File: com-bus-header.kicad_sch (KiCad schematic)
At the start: 10 parts, among them IC6 SN75C3232EPWR, J2 67996-110HLF

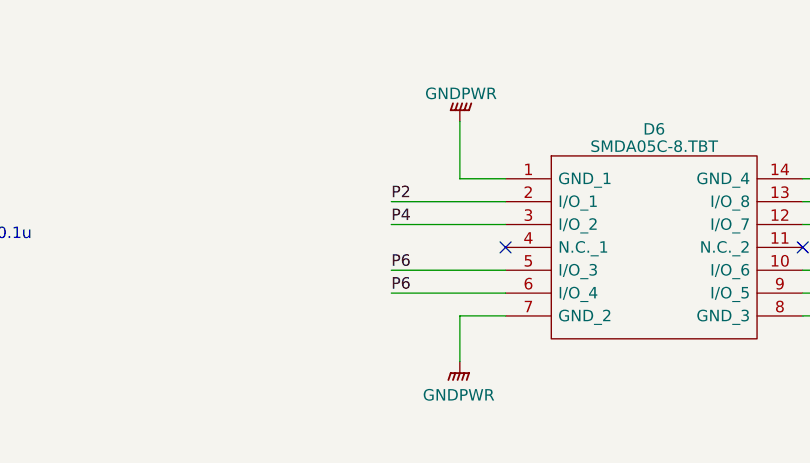
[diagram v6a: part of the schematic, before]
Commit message: initial component layout
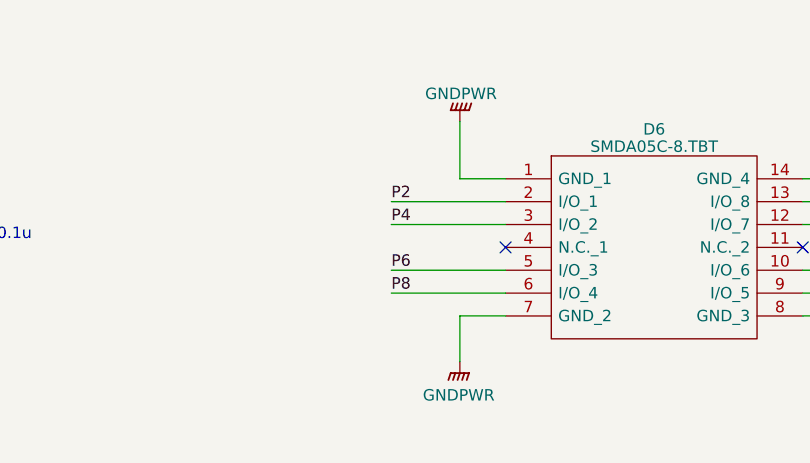
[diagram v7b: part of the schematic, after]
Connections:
- net P6: no longer D6.6 (I/O_4)
- net P8: now also D6.6 (I/O_4)
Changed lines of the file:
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@@
     (effects (font (size 1.27 1.27)) (justify left bottom))
   )
-  (label "P6" (at 168.275 137.795 0) (fields_autoplaced)
+  (label "P8" (at 168.275 137.795 0) (fields_autoplaced)
     (effects (font (size 1.27 1.27)) (justify left bottom))
   )
@@
   (symbol (lib_id "power:GND") (at 165.1 97.79 0) (unit 1)
     (in_bom yes) (on_board yes) (dnp no) (fields_autoplaced)
-    (property "Reference" "#PWR080" (at 165.1 104.14 0)
+    (property "Reference" "#PWR078" (at 165.1 104.14 0)
       (effects (font (size 1.27 1.27)) hide)
     )
@@
       (project "Oro Link rev2"
         (path "/e89dcd22-1250-4a5b-b778-1c95a0dd623d/a5104146-06a0-496e-bda0-1e4731a261c3"
-          (reference "#PWR080") (unit 1)
+          (reference "#PWR078") (unit 1)
         )
       )
@@
   (symbol (lib_id "power:GND") (at 113.03 73.66 0) (unit 1)
     (in_bom yes) (on_board yes) (dnp no) (fields_autoplaced)
-    (property "Reference" "#PWR078" (at 113.03 80.01 0)
+    (property "Reference" "#PWR076" (at 113.03 80.01 0)
       (effects (font (size 1.27 1.27)) hide)
     )
@@
       (project "Oro Link rev2"
         (path "/e89dcd22-1250-4a5b-b778-1c95a0dd623d/a5104146-06a0-496e-bda0-1e4731a261c3"
-          (reference "#PWR078") (unit 1)
+          (reference "#PWR076") (unit 1)
         )
       )
@@
         )
         (path "/e89dcd22-1250-4a5b-b778-1c95a0dd623d/a5104146-06a0-496e-bda0-1e4731a261c3"
-          (reference "#PWR082") (unit 1)
+          (reference "#PWR080") (unit 1)
         )
       )
@@
   (symbol (lib_id "power:GND") (at 118.11 149.225 0) (unit 1)
     (in_bom yes) (on_board yes) (dnp no) (fields_autoplaced)
-    (property "Reference" "#PWR079" (at 118.11 155.575 0)
+    (property "Reference" "#PWR077" (at 118.11 155.575 0)
       (effects (font (size 1.27 1.27)) hide)
     )
@@
       (project "Oro Link rev2"
         (path "/e89dcd22-1250-4a5b-b778-1c95a0dd623d/a5104146-06a0-496e-bda0-1e4731a261c3"
-          (reference "#PWR079") (unit 1)
+          (reference "#PWR077") (unit 1)
         )
       )
@@
         )
         (path "/e89dcd22-1250-4a5b-b778-1c95a0dd623d/a5104146-06a0-496e-bda0-1e4731a261c3"
-          (reference "#PWR084") (unit 1)
+          (reference "#PWR082") (unit 1)
         )
       )
@@
         )
         (path "/e89dcd22-1250-4a5b-b778-1c95a0dd623d/a5104146-06a0-496e-bda0-1e4731a261c3"
-          (reference "#PWR081") (unit 1)
+          (reference "#PWR079") (unit 1)
         )
       )
@@
   (symbol (lib_id "power:+3V3") (at 104.14 74.93 0) (unit 1)
     (in_bom yes) (on_board yes) (dnp no) (fields_autoplaced)
-    (property "Reference" "#PWR077" (at 104.14 78.74 0)
+    (property "Reference" "#PWR075" (at 104.14 78.74 0)
       (effects (font (size 1.27 1.27)) hide)
     )
@@
       (project "Oro Link rev2"
         (path "/e89dcd22-1250-4a5b-b778-1c95a0dd623d/a5104146-06a0-496e-bda0-1e4731a261c3"
-          (reference "#PWR077") (unit 1)
+          (reference "#PWR075") (unit 1)
         )
       )
@@
   (symbol (lib_id "power:+3V3") (at 90.17 144.145 0) (unit 1)
     (in_bom yes) (on_board yes) (dnp no) (fields_autoplaced)
-    (property "Reference" "#PWR076" (at 90.17 147.955 0)
+    (property "Reference" "#PWR074" (at 90.17 147.955 0)
       (effects (font (size 1.27 1.27)) hide)
     )
@@
       (project "Oro Link rev2"
         (path "/e89dcd22-1250-4a5b-b778-1c95a0dd623d/a5104146-06a0-496e-bda0-1e4731a261c3"
-          (reference "#PWR076") (unit 1)
+          (reference "#PWR074") (unit 1)
         )
       )
@@
         )
         (path "/e89dcd22-1250-4a5b-b778-1c95a0dd623d/a5104146-06a0-496e-bda0-1e4731a261c3"
-          (reference "D14") (unit 1)
+          (reference "D16") (unit 1)
         )
       )
@@
         )
         (path "/e89dcd22-1250-4a5b-b778-1c95a0dd623d/a5104146-06a0-496e-bda0-1e4731a261c3"
-          (reference "#PWR083") (unit 1)
-        )
-      )
+          (reference "#PWR081") (unit 1)
+        )
+      )
